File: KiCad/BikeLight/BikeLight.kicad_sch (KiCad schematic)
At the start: 62 parts, among them J1 Conn-01x02_P2.5mm_S2B-XH-A-BK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, J2 Conn-01x02_P2.5mm_S2B-XH-A-BK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, J3 GT-USB-7051A, J4 Conn-01x02_P2.5mm_S2B-XH-A-BK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, J5 Conn-01x02_P2.5mm_S2B-XH-A-BK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, Q1 AO3401A, Q2 BC337, Q3 BC337, SW1 CK_KMS2xxG, U1 TP4056-42-ESOP8, U2 MT3608, U3 MAX17048, U4 MCP1826S-33, U5 HT-CT62, U6 RFID-RC522, U7 MPU-6050, U8 PCA9555DB

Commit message: Comenting files
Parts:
- added Q2: AO3400A, Package_TO_SOT_SMD:SOT-23, symbol 00-kiml-transistor-fet:AO3400A
- renumbered C10 to C1, C11 to C10, C8 to C11, C3 to C2, C2 to C3, C5 to C4, C7 to C5, C9 to C6, C1 to C7, C4 to C8, C6 to C9, D3 to D2, D2 to D3, J2 to J1, J1 to J2, Q2 to Q3, Q3 to Q4, R22 to R1, R13 to R10, R23 to R11, R24 to R12, R14 to R13, R25 to R14, R1 to R15, R2 to R16, R7 to R17, R8 to R18, R27 to R19, R21 to R2, R28 to R20, R9 to R21, R17 to R22, R18 to R23, R10 to R24, R11 to R25, R12 to R26, R29 to R27, R30 to R28, R15 to R3, R16 to R4, R26 to R5, R3 to R6, R6 to R7, R4 to R8, R5 to R9, U7 to U2, U6 to U5, U2 to U6, U8 to U7, U5 to U8
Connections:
- net +3.3V: now also Q2.3 (D)
- net BUSSER: now also Q2.1 (G)
- net GND: now also BZ1.2 (-), U1.3 (OUT-)
- net LED: now also R27.2, R28.1
- net at BZ1.1 (+): now also Q2.2 (S)
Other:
- added sheet Accelerometer (Accelerometer.kicad_sch)
- added sheet Charger (Charger.kicad_sch)
- added sheet Fuel Gauge (FuelGauge.kicad_sch)
- added sheet GPIO-extender (GPIO-extender.kicad_sch)
- added sheet Light and buzzer (Light.kicad_sch)
- added sheet MCU (MCU.kicad_sch)
- added sheet Power Supply (PowerSupply.kicad_sch)
- added sheet RFID (RFID.kicad_sch)
- added sheet Solar Boost (SolarBoost.kicad_sch)
- added sheet USB Programing (USBPrograming.kicad_sch)
- moved on the sheet: BZ1, C1, C10, C11, C2, C3, C4, C5, C6, C7, C8, C9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

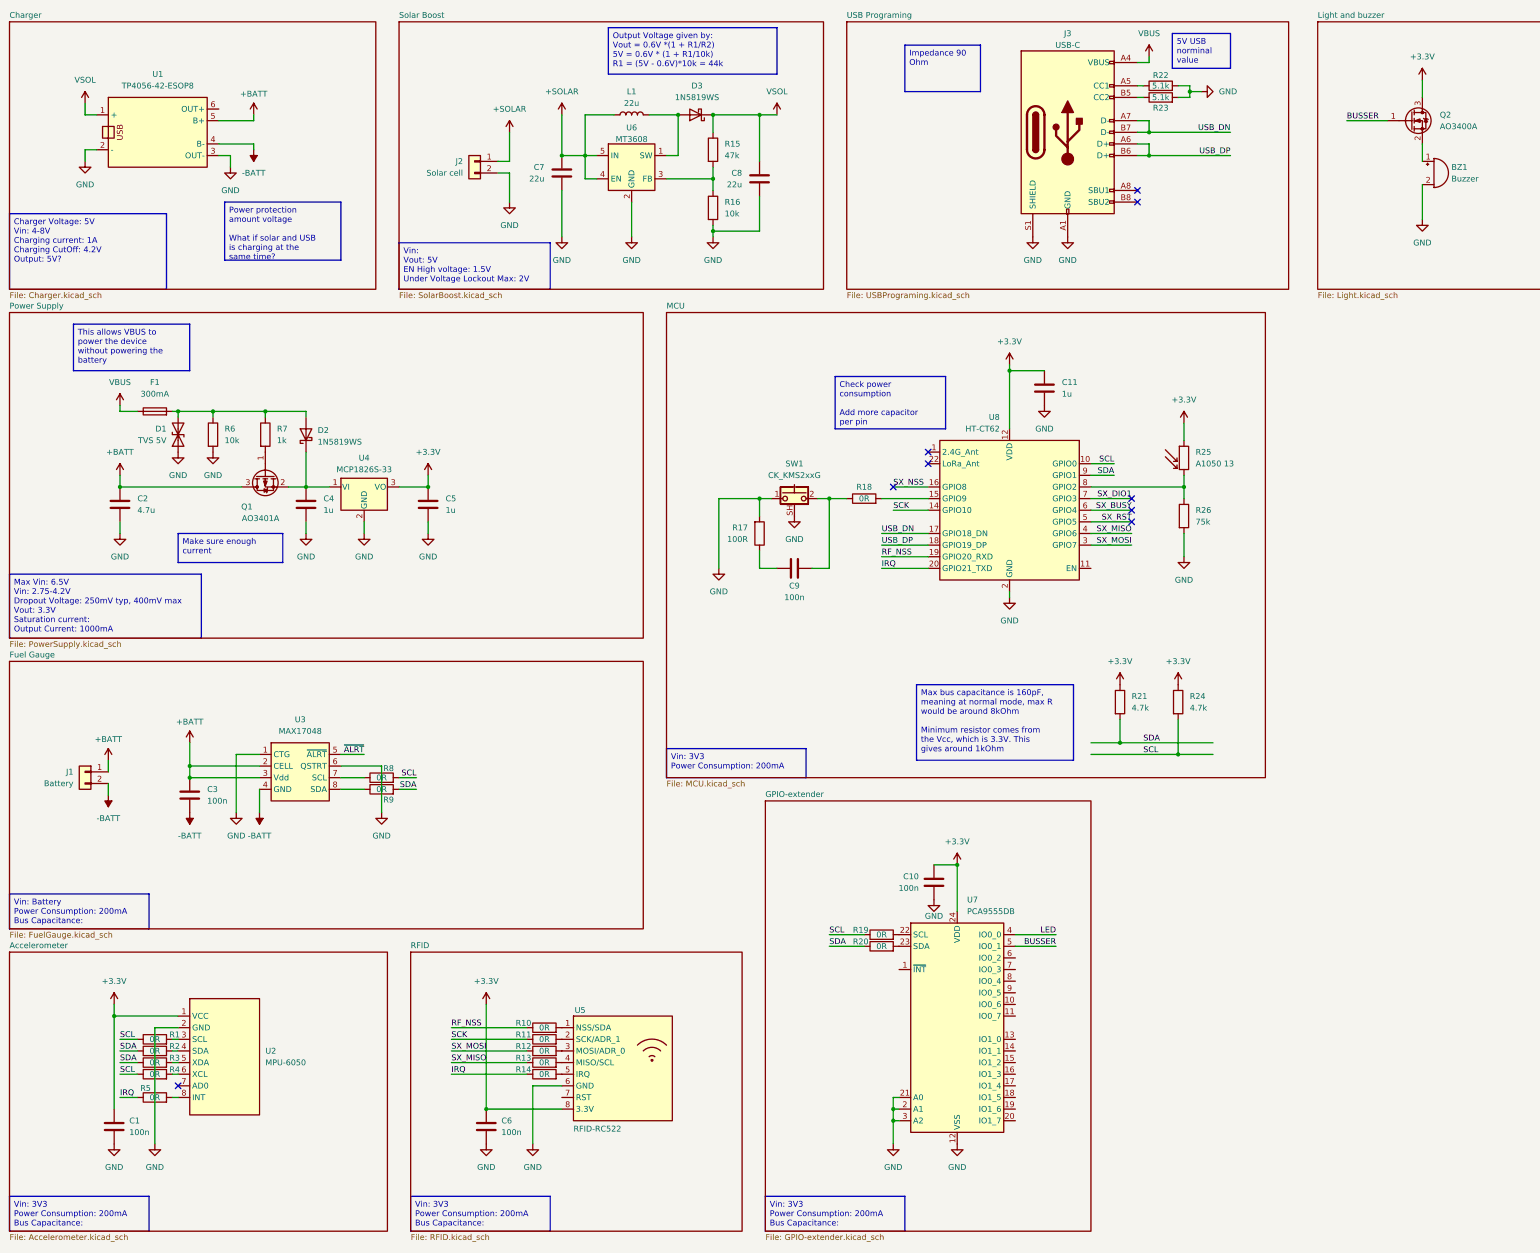
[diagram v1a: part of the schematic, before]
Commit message: Changing GPIO pins
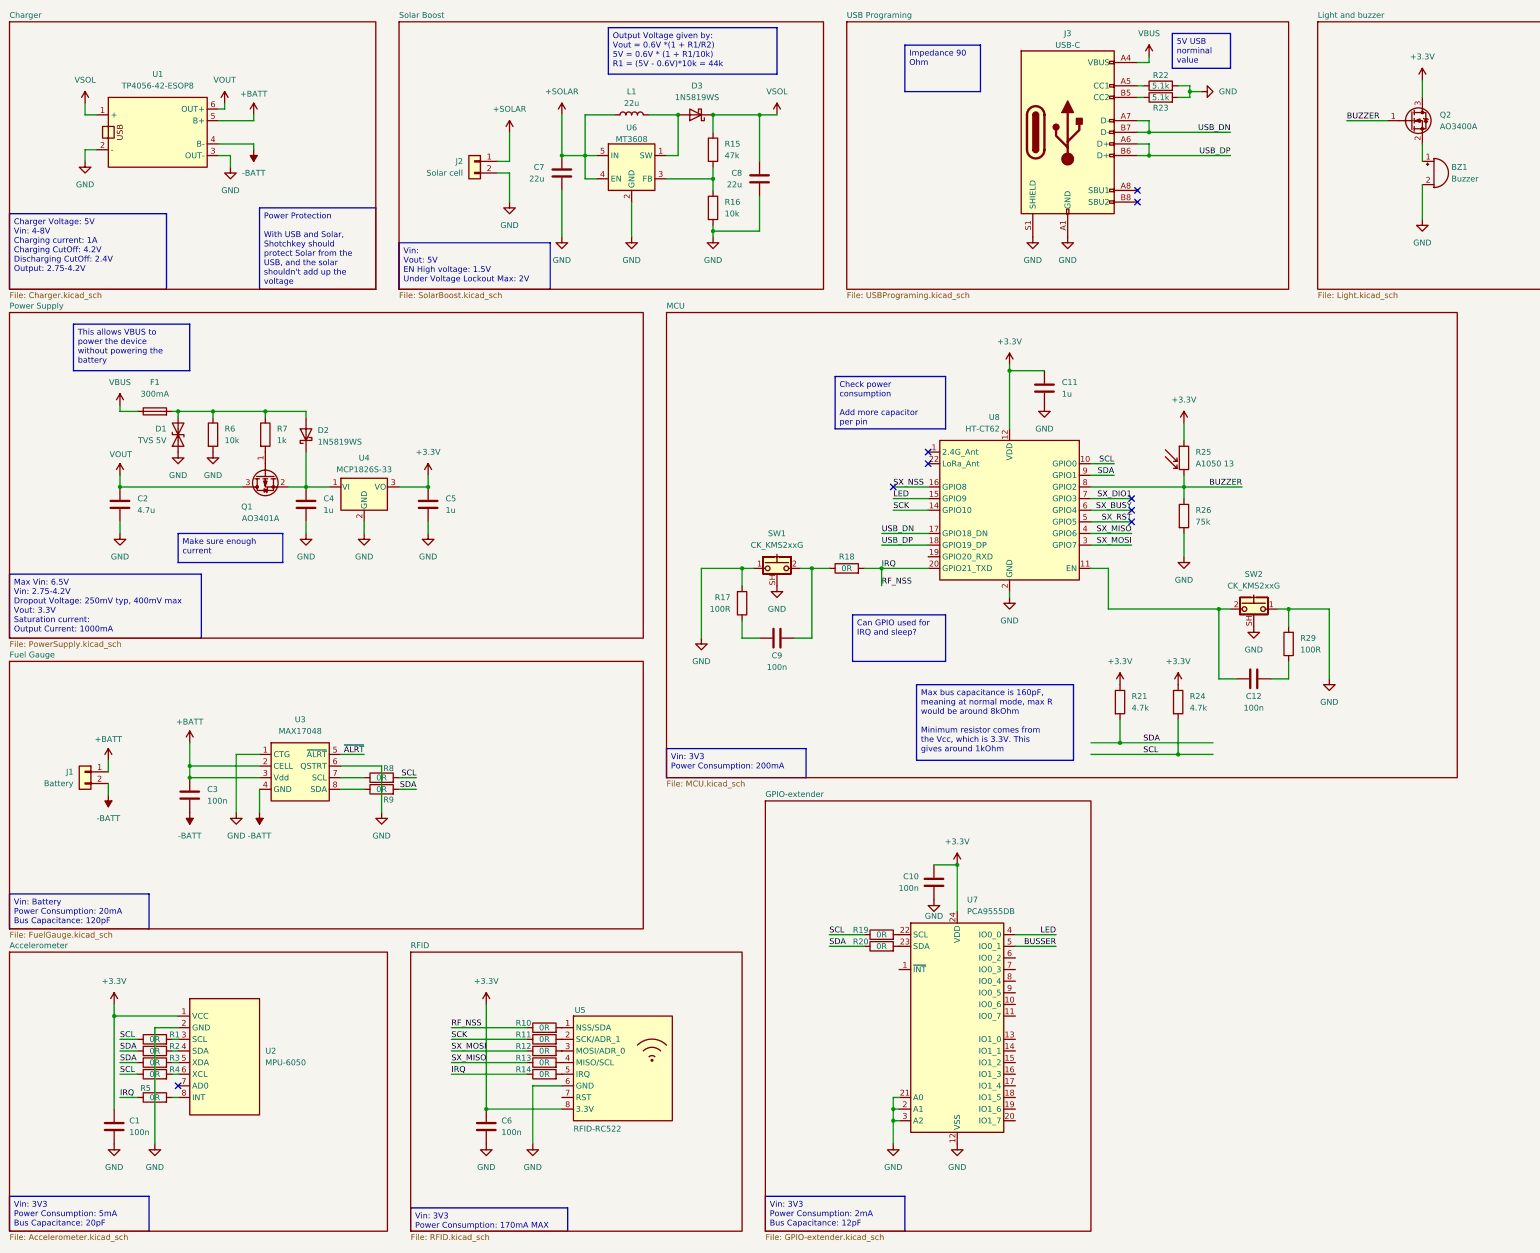
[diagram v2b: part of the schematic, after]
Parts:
- added C12: 100n_0603_TCC0603X7R104K500CT, Capacitor_SMD:C_0603_1608Metric, symbol 00-kiml-capacitors-smd:100n_0603_TCC0603X7R104K500CT
- added R29: 100R_0603_RC0603FR-07100RL, Resistor_SMD:R_0603_1608Metric, symbol 00-kiml-resistors-smd:100R_0603_RC0603FR-07100RL
- added SW2: CK_KMS2xxG, Button_Switch_SMD:SW_SPST_CK_KMS2xxGP, symbol Switch:CK_KMS2xxG
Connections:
- net +BATT: no longer C2.1, Q1.3 (D)
- net BUSSER: no longer Q2.1 (G)
- net GND: now also R29.2, SW2.1, SW2.SH (B)
- net IRQ: now also R10.1, R18.2
- net LED: now also U8.15 (GPIO9)
- net at U8.11 (EN): now also C12.2, SW2.2
- net BUZZER: now reaches R25.2, R26.1, U8.8 (GPIO2)
- net BUZZER: now also Q2.1 (G)
- net VOUT: now reaches U1.6 (OUT+)
- net VOUT: now also C2.1, Q1.3 (D)
- net RF_NSS: no longer names the net of U8.19 (GPIO20_RXD)
- net RF_NSS: no longer R10.1
- new net: C12.1, R29.1
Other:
- moved on the sheet: C9, R17, R18, SW1

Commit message: Gerber generation
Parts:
- removed D1: SOD-882_0402_RCLAMP0521P-N, Diode_SMD:D_0402_1005Metric, symbol 00-kiml-power-protection:SOD-882_0402_RCLAMP0521P-N
- removed Q3, Q4: BC337, Package_TO_SOT_THT:TO-92_Inline, symbol Transistor_BJT:BC337
- removed SW1, SW2: CK_KMS2xxG, Button_Switch_SMD:SW_SPST_CK_KMS2xxGP, symbol Switch:CK_KMS2xxG
- added D4: SMAJ5.0CA/TR13_NONAME, Diode_SMD:D_SMA, symbol Personal_Library:SMAJ5.0CA/TR13_NONAME
- added J6: Conn_01x05, Connector_PinHeader_2.54mm:PinHeader_1x05_P2.54mm_Horizontal, symbol Connector_Generic:Conn_01x05
- added Q3: BC847BDW1, Package_TO_SOT_SMD:SOT-363_SC-70-6, symbol Transistor_BJT:BC847BDW1
- added R19, R31: 100k_0603_RC0603FR-07100KL, Resistor_SMD:R_0603_1608Metric, symbol 00-kiml-resistors-smd:100k_0603_RC0603FR-07100KL
- added SW2: SW_PB_B3F-4055, 00-kiml-switch-button-tht:SW_PB_B3F-4055, symbol 00-kiml-switch-button-smd:SW_PB_B3F-4055
- added SW3: K2-1102AQ-H4CW-01, Personal_Library:SW_Tactile_SPST_Angled_K2-1102AQ-H4CW-01, symbol Personal_Library:SW_K2-1102AQ-H4CW-01
- renumbered R19 to R20, R20 to R21, R21 to R22, R22 to R23, R23 to R24, R24 to R25, R25 to R26, R26 to R27, R29 to R28, R27 to R29, R28 to R30
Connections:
- net +3.3V: now also J6.1 (VCC), Q3.3 (C2), Q3.6 (C1), R19.1, R31.1
- net GND: now also D4.1 (A1), J6.2 (GND), SW2.2, SW3.1
- net IRQ: now also R19.2
- net at R30.2: now also Q3.2 (B1)
- net at J4.1 (Pin_1): now also Q3.4 (E2)
- net at D2.2 (A), F1.2, R6.1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: now also D4.2 (A2)
- net at C9.2, R18.1: now also SW3.2
- net at J5.1 (Pin_1): now also Q3.1 (E1)
- net at R29.1: now also Q3.5 (B2)
- net at C12.2, U8.11 (EN): now also R31.2, SW2.1
- net GNSS_RX: now reaches U8.19 (GPIO20_RXD)
- net GNSS_RX: now also J6.3 (TXD)
- no-connect marks 9 -> 11
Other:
- removed sheet Accelerometer
- removed sheet Charger
- removed sheet Fuel Gauge
- removed sheet GPIO-extender
- removed sheet Light and buzzer
- removed sheet MCU
- removed sheet Power Supply
- removed sheet RFID
- removed sheet Solar Boost
- removed sheet USB Programing
- moved on the sheet: C12, R18, R28

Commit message: Changing pins
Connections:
- net GNSS_RX: no longer U8.19 (GPIO20_RXD)
- net IRQ: now also U8.15 (GPIO9); no longer U8.20 (GPIO21_TXD)
- net LED: now also U8.20 (GPIO21_TXD); no longer U8.15 (GPIO9)
- net SCK: now also U8.19 (GPIO20_RXD); no longer U8.14 (GPIO10)
- net SCL: now also U8.17 (GPIO18_DN); no longer U8.10 (GPIO0)
- net SDA: now also U8.18 (GPIO19_DP); no longer U8.9 (GPIO1)
- net USB_DN: no longer U8.17 (GPIO18_DN)
- net USB_DP: no longer U8.18 (GPIO19_DP)
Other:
- moved on the sheet: C9, R17, R18, R19, SW3

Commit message: Small updates to pins
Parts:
- removed C10: 100n_0603_TCC0603X7R104K500CT, Capacitor_SMD:C_0603_1608Metric, symbol 00-kiml-capacitors-smd:100n_0603_TCC0603X7R104K500CT
- removed R20, R21: 0R_0603_0603WAF0000T5E, Resistor_SMD:R_0603_1608Metric, symbol 00-kiml-resistors-smd:0R_0603_0603WAF0000T5E
- removed U7: PCA9555DB, Package_SO:SSOP-24_5.3x8.2mm_P0.65mm, symbol Interface_Expansion:PCA9555DB
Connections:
- net GNSS_RX: now also U8.19 (GPIO20_RXD)
- net SCK: now also U8.14 (GPIO10); no longer U8.19 (GPIO20_RXD)
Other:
- company: (none) -> Group 1
- moved on the sheet: C1, C2, C4, C5, C6, D2, D4, F1, J3, J4, J5, Q1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

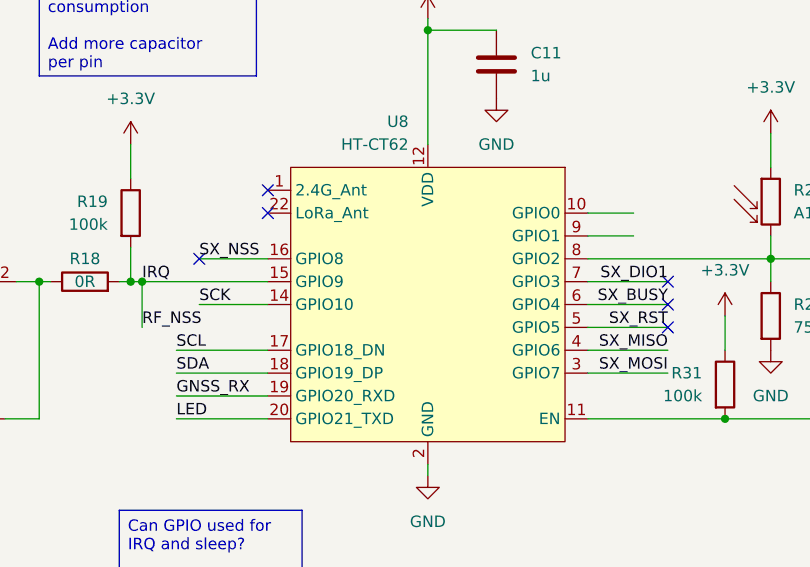
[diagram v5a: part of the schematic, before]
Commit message: Changed and updated 3D models of devices
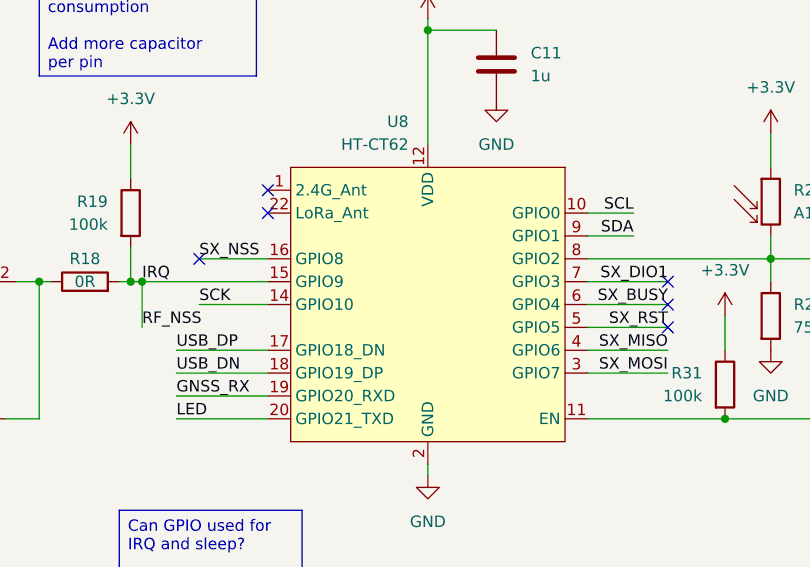
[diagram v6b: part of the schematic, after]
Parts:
- J3: footprint Connector_USB:USB_C_Receptacle_G-Switch_GT-USB-7051x -> JLC2KICAD_Library:USB-C-SMD_GT-USB-7051A
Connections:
- net SCL: now also U8.10 (GPIO0); no longer U8.17 (GPIO18_DN)
- net SDA: now also U8.9 (GPIO1); no longer U8.18 (GPIO19_DP)
- net USB_DN: now also U8.18 (GPIO19_DP)
- net USB_DP: now also U8.17 (GPIO18_DN)
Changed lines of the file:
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@@
+		)
+	)
+	(label "USB_DN"
+		(at 205.74 130.81 0)
+		(effects
+			(font
+				(size 1.27 1.27)
+			)
+			(justify left bottom)
 		)
 	)
@@
 		)
 	)
+	(label "USB_DP"
+		(at 205.74 128.27 0)
+		(effects
+			(font
+				(size 1.27 1.27)
+			)
+			(justify left bottom)
+		)
+	)
 	(label "RF_NSS"
 		(at 201.93 125.73 0)
@@
 		)
 	)
+	(label "SDA"
+		(at 256.54 115.57 180)
+		(effects
+			(font
+				(size 1.27 1.27)
+			)
+			(justify right bottom)
+		)
+	)
 	(label "RF_NSS"
 		(at 111.76 240.03 0)
@@
 		)
 	)
-	(label "SCL"
-		(at 205.74 128.27 0)
-		(effects
-			(font
-				(size 1.27 1.27)
-			)
-			(justify left bottom)
-		)
-	)
 	(label "USB_DP"
 		(at 289.56 50.8 180)
@@
 		)
 	)
-	(label "SDA"
-		(at 205.74 130.81 0)
-		(effects
-			(font
-				(size 1.27 1.27)
-			)
-			(justify left bottom)
-		)
-	)
 	(label "~{ALRT}"
 		(at 92.71 176.53 180)
@@
 			)
 			(justify left bottom)
+		)
+	)
+	(label "SCL"
+		(at 256.54 113.03 180)
+		(effects
+			(font
+				(size 1.27 1.27)
+			)
+			(justify right bottom)
 		)
 	)
@@
 			)
 		)
-		(property "Footprint" "Connector_USB:USB_C_Receptacle_G-Switch_GT-USB-7051x"
+		(property "Footprint" "JLC2KICAD_Library:USB-C-SMD_GT-USB-7051A"
 			(at 254 8.89 0)
 			(effects

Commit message: Updating sch and pcb
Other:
- company: Group 1 -> DTU Group 1
- title: Bikelight -> BeamBuddy
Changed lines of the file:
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@@
 	(paper "A3")
 	(title_block
-		(title "Bikelight")
-		(date "2025-05-21")
-		(company "Group 1")
+		(title "BeamBuddy")
+		(date "2025-05-24")
+		(company "DTU Group 1")
 	)
 	(text_box "Charger"
